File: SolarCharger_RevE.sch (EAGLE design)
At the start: 134 parts, among them CON1 CON_4X200MIL, CON2 USB_BMULTICOMP, CON3 ICSP, CON4 CON_3X100MIL, CON5 CON_3X100MIL, CON6 CON_8X200MIL, CON7 CON_2X100MIL, CON8 CON_3X100MIL, CON9 CON_6X3X2, IC1 MCP3428, IC10 AT45DB161E, IC11 TPS54428, IC12 MCP14A0153, IC13 MCP14A0153, IC2 INA213, IC3 MIC4605-1YM, IC4 INA213, IC5 PIC18F46J50, IC6 TS6001, IC7 LMT86, IC8 24AA16, IC9 TPS62120, Q1 NX3008NBKW, Q10 NTR4101PT1G, Q11 N-FET, Q12 N-FET, Q13 N-FET, Q14 N-FET, Q15 NX3008NBKW, Q2 PSMN6R0-30YL, Q3 NX3008NBKW, Q4 NTR4101PT1G, Q5 PSMN6R0-30YL, Q6 PSMN6R0-30YL, Q7 NX3008NBKW, Q8 NX3008NBKW, Q9 NX3008NBKW, X1 ABS07-120-32.768KHZ-T, X2 ABM3-8.000MHZ-D2Y-T, X3 USB_A, X4 USB_A

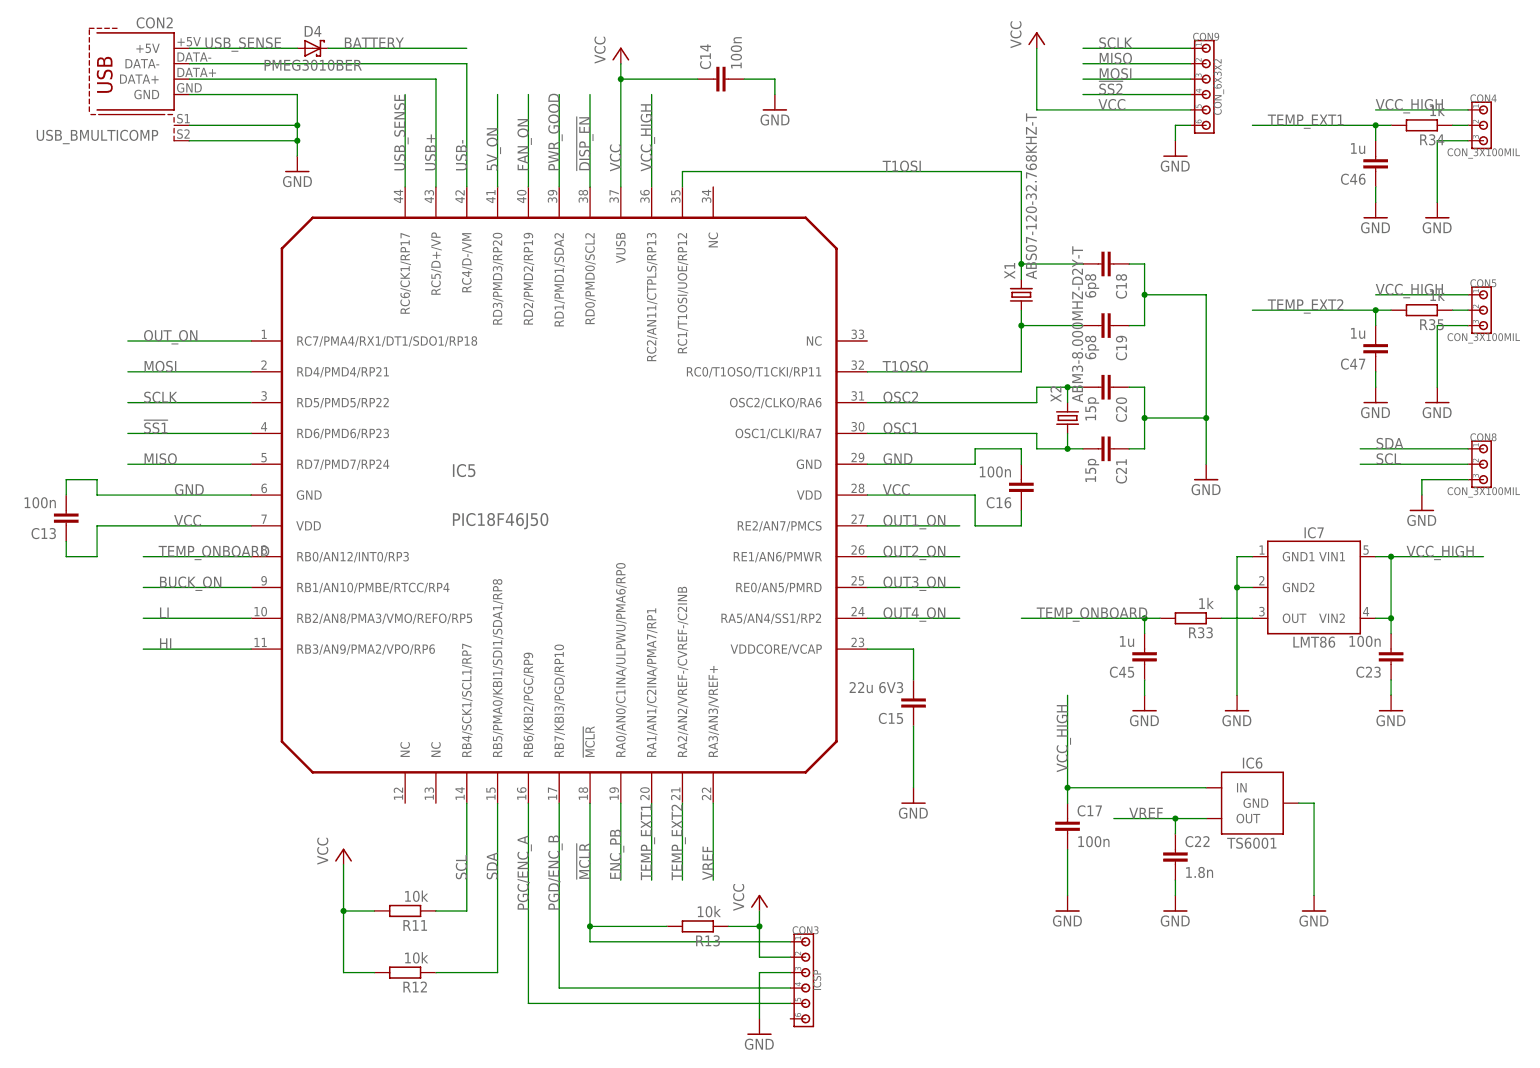
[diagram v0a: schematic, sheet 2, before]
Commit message: Revision E completed. Now with SPI and I2C headers
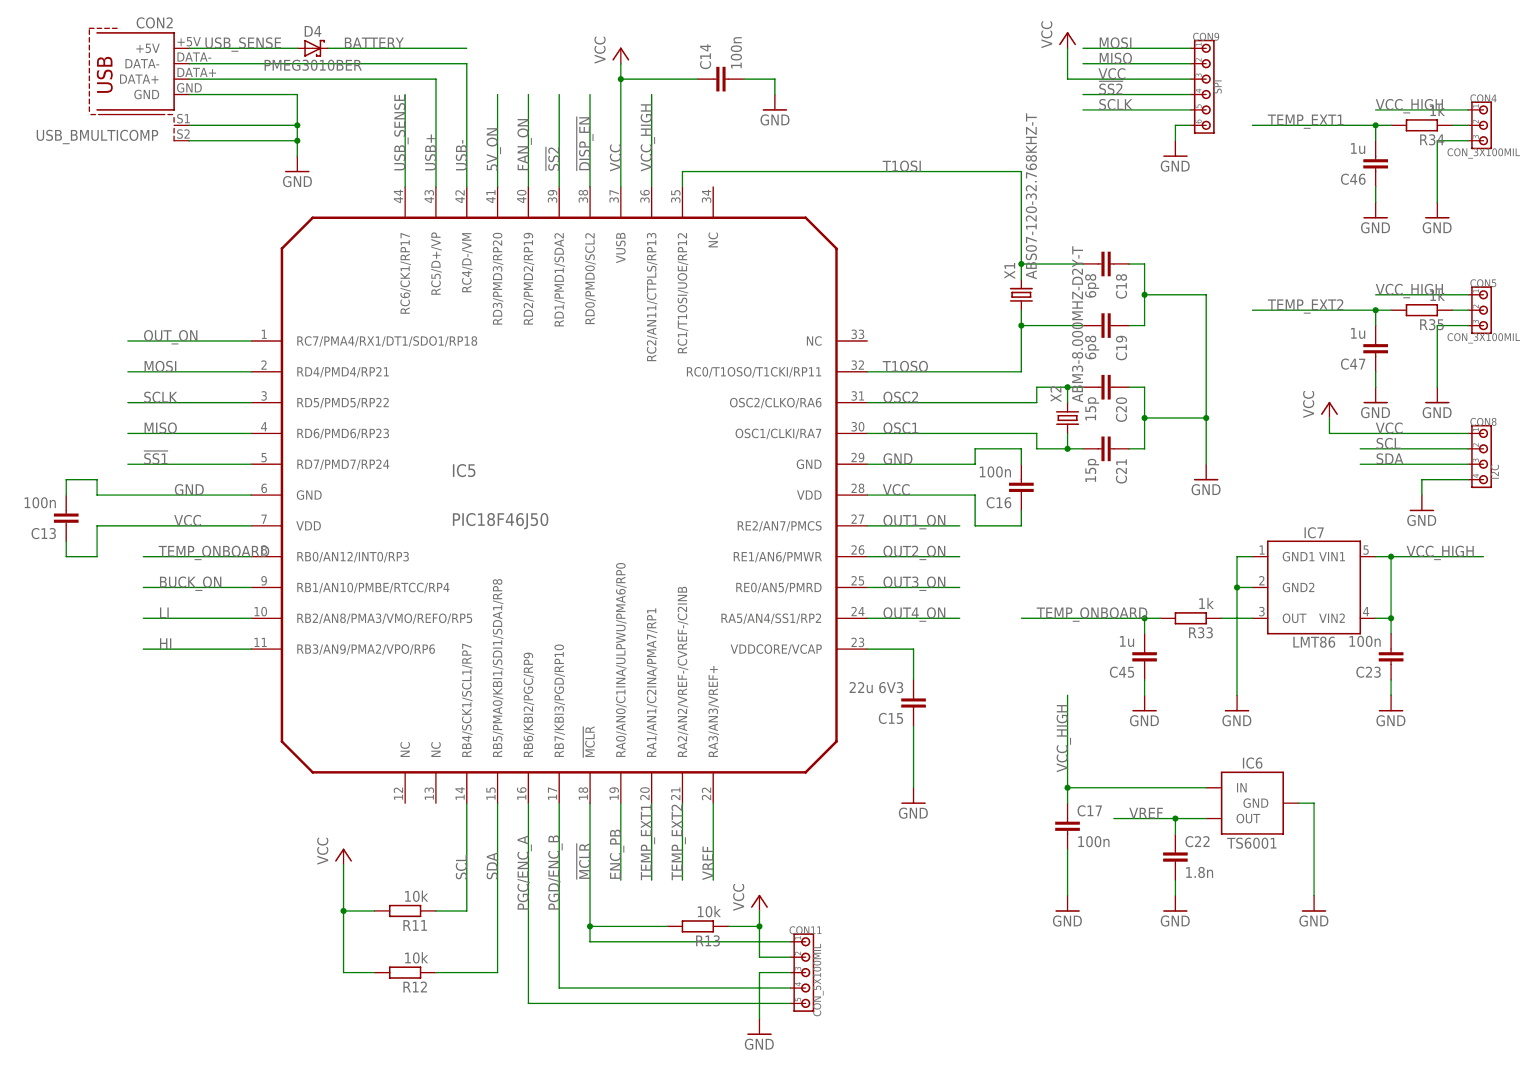
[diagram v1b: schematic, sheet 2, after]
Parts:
- removed CON3: ICSP, 00Connector:CON_6X100MIL
- removed R15: 100k, 00Resistor:RESISTORR0805
- added CON11: CON_5X100MIL, 00Connector:CON_5X100MIL
- CON8: value CON_3X100MIL -> I2C; device 00Connector:CON_3X100MIL -> 00Connector:CON_4X100MIL
- CON9: value CON_6X3X2 -> SPI
- IC10: value AT45DB161E -> AT45DB321E; device 00Logic:AT45DB161E -> 00Logic:AT45DB161EEIAJ
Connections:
- removed net PWR_GOOD: IC5.RD1/PMD1/SDA2, IC9.PG, R15.2
- net !MCLR!: now also CON11.1; no longer CON3.1
- net !SS1!: now also IC5.RD7/PMD7/RP24; no longer IC5.RD6/PMD6/RP23
- net !SS2!: now also IC5.RD1/PMD1/SDA2
- net GND: now also CON11.3, CON8.4; no longer CON3.3, CON8.3
- net MISO: now also IC5.RD6/PMD6/RP23; no longer IC5.RD7/PMD7/RP24
- net MOSI: now also CON9.1; no longer CON9.3
- net PGC/ENC_A: now also CON11.5; no longer CON3.5
- net PGD/ENC_B: now also CON11.4; no longer CON3.4
- net SCLK: now also CON9.5; no longer CON9.1
- net SDA: now also CON8.3; no longer CON8.1
- net VCC: now also CON11.2, CON8.1, CON9.3; no longer CON3.2, CON9.5, R15.1

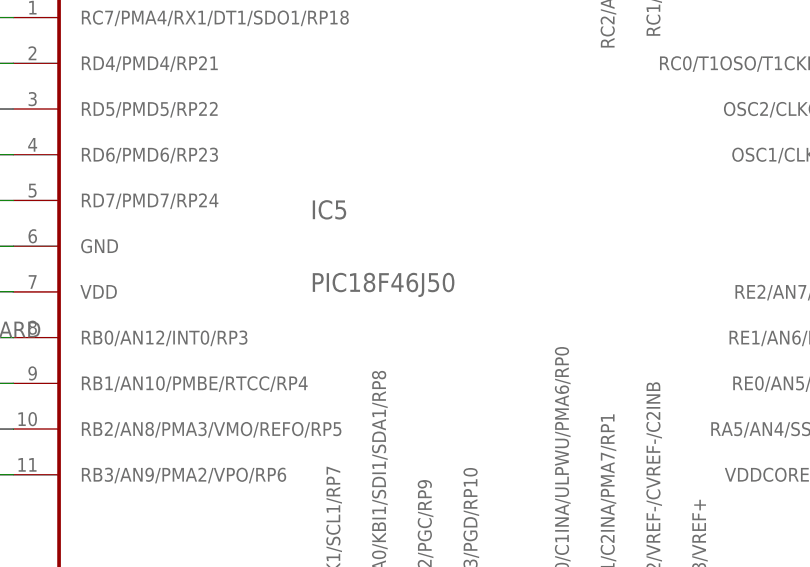
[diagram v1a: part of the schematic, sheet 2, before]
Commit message: Some final minor changes. Moved a capacitor, re-routed a VCC trace. Gerbers exported as ordered
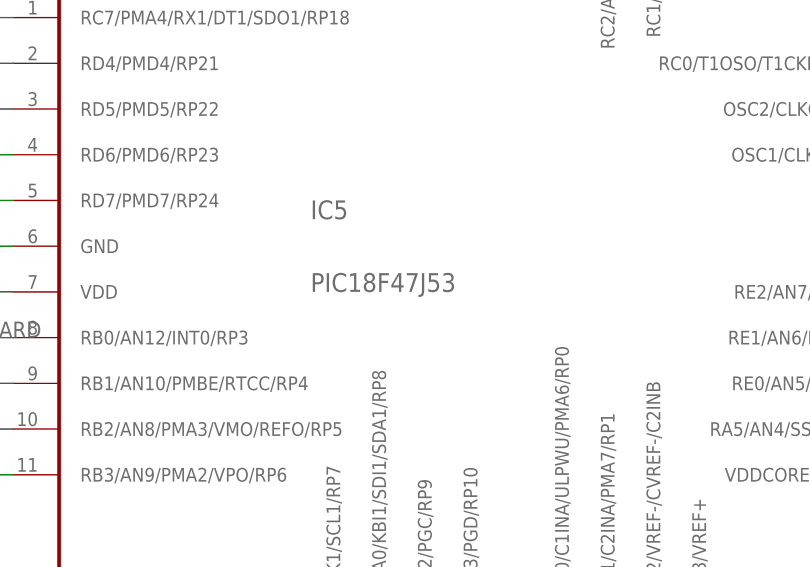
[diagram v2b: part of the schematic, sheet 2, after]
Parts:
- IC5: value PIC18F46J50 -> PIC18F47J53
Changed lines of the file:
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@@
 <part name="Q3" library="00Mosfet" deviceset="N-FET" device="SOT23" value="NX3008NBKW"/>
 <part name="R6" library="00Resistor" deviceset="RESISTOR" device="R0805" value="5R6"/>
-<part name="IC5" library="00PIC" deviceset="PIC18F46J50" device=""/>
+<part name="IC5" library="00PIC" deviceset="PIC18F46J50" device="" value="PIC18F47J53"/>
 <part name="X2" library="00Crystal" deviceset="CRYSTAL" device="5X3.2MM" value="ABM3-8.000MHZ-D2Y-T"/>
 <part name="P+5" library="supply1" deviceset="VCC" device=""/>

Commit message: Revision F: Just swapped 2 signals
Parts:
- C22: value 1.8n -> 1u
- IC6: value TS6001 -> TI_REF2925
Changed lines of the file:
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@@
 <part name="P+1" library="supply1" deviceset="VCC" device=""/>
 <part name="CON4" library="00Connector" deviceset="CON_3X" device="100MIL"/>
-<part name="IC6" library="00VoltageReference" deviceset="TS6001" device=""/>
+<part name="IC6" library="00VoltageReference" deviceset="TS6001" device="" value="TI_REF2925"/>
 <part name="GND29" library="00Supply" deviceset="GND" device=""/>
 <part name="P+7" library="supply1" deviceset="VCC" device=""/>
 <part name="P+8" library="supply1" deviceset="VCC" device=""/>
-<part name="C22" library="00Capacitor" deviceset="C" device="C0805" value="1.8n"/>
+<part name="C22" library="00Capacitor" deviceset="C" device="C0805" value="1u"/>
 <part name="GND30" library="00Supply" deviceset="GND" device=""/>
 <part name="R10" library="00Resistor" deviceset="RESISTOR" device="R0805" value="300k"/>
